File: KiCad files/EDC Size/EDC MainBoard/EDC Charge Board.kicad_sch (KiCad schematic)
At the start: 38 parts, among them IC2 TPS25730SRSMR, J1 USB_C_Receptacle_USB2.0_16P, J2 Conn_01x06, Q1 CSD87501L

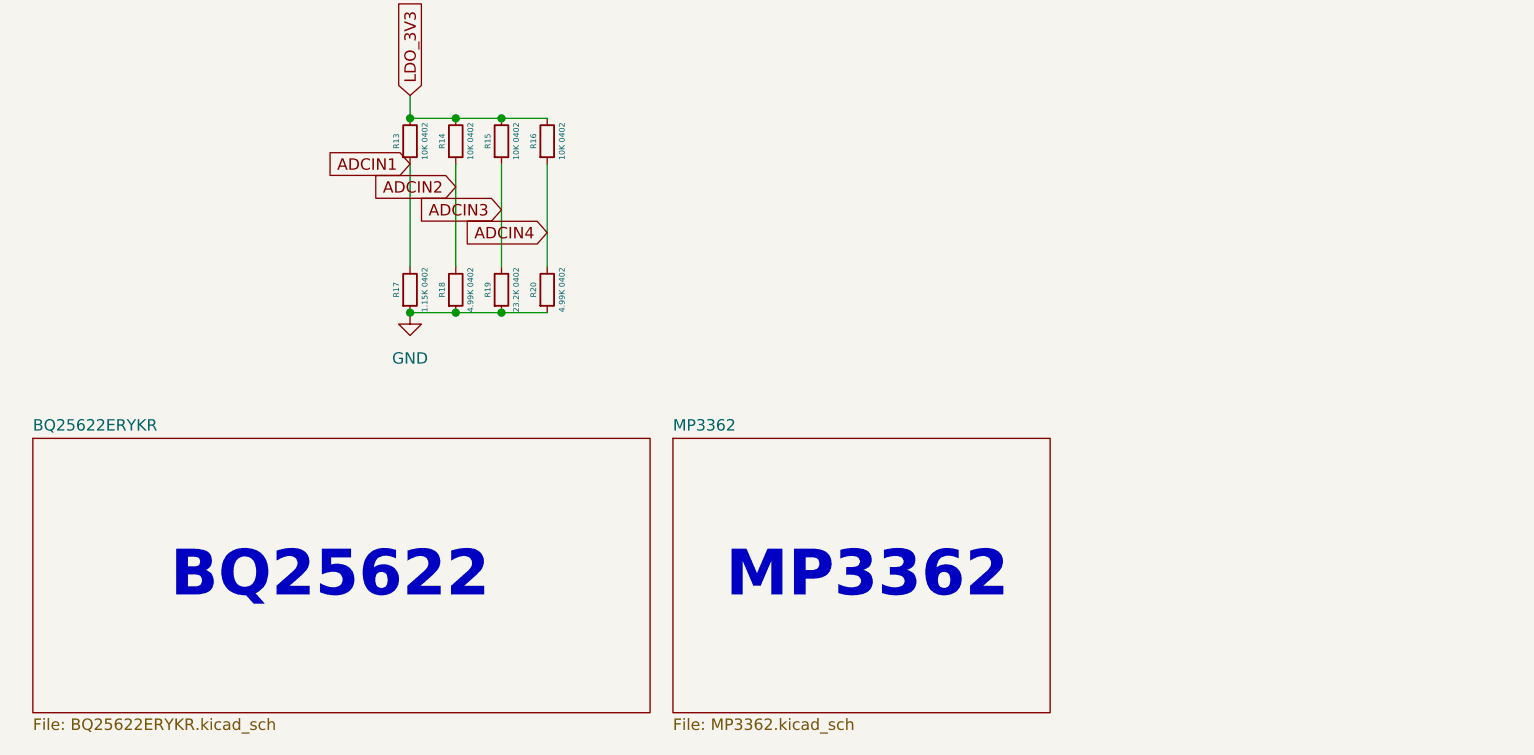
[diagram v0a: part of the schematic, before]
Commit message: updated the schematics and completed the battery charge IC circuit
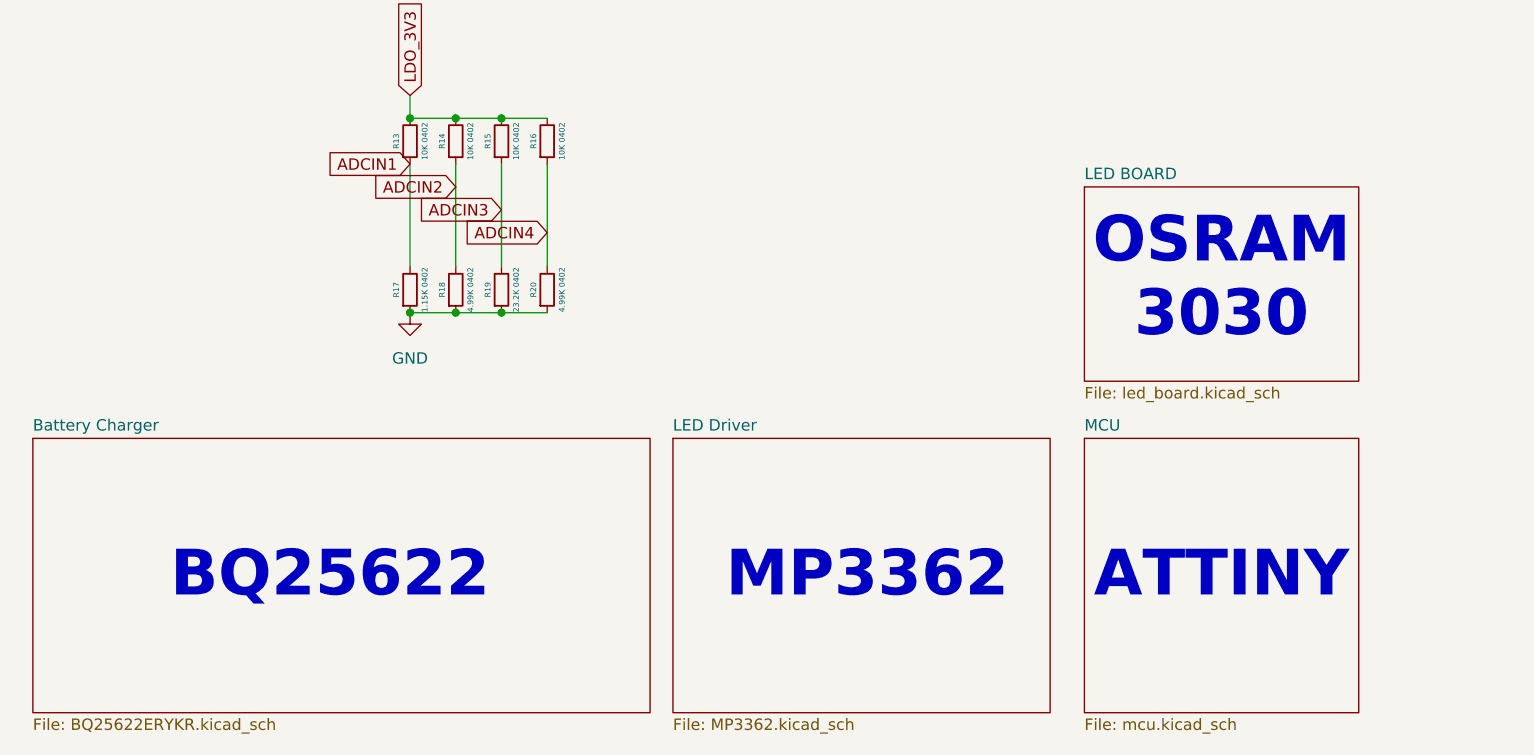
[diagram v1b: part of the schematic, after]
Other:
- sheet BQ25622ERYKR renamed Battery Charger
- sheet MP3362 renamed LED Driver
- added sheet LED BOARD (led_board.kicad_sch)
- added sheet MCU (mcu.kicad_sch)
- note added: "ATTINY"
- note added: "OSRAM 3030"
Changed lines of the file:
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@@
 		)
 	)
+	(text "OSRAM\n3030"
+		(exclude_from_sim no)
+		(at 149.86 139.7 0)
+		(effects
+			(font
+				(size 5.08 5.08)
+				(thickness 1.016)
+				(bold yes)
+			)
+		)
+	)
 	(text "MP3362"
 		(exclude_from_sim no)
@@
 		)
 	)
+	(text "ATTINY"
+		(exclude_from_sim no)
+		(at 149.86 172.72 0)
+		(effects
+			(font
+				(size 5.08 5.08)
+				(thickness 1.016)
+				(bold yes)
+			)
+		)
+	)
 	(text "BQ25622"
 		(exclude_from_sim no)
@@
 	(label "FAULT_IN"
 		(at 121.92 63.5 180)
-		(fields_autoplaced yes)
 		(effects
 			(font
@@
 	(label "FAULT_IN"
 		(at 251.46 55.88 0)
-		(fields_autoplaced yes)
 		(effects
 			(font
@@
 			(color 0 0 0 0.0000)
 		)
-		(property "Sheetname" "BQ25622ERYKR"
+		(property "Sheetname" "Battery Charger"
 			(at 17.78 156.7684 0)
 			(effects
@@
 	)
 	(sheet
+		(at 134.62 129.54)
+		(size 30.48 21.59)
+		(fields_autoplaced yes)
+		(stroke
+			(width 0.1524)
+			(type solid)
+		)
+		(fill
+			(color 0 0 0 0.0000)
+		)
+		(property "Sheetname" "LED BOARD"
+			(at 134.62 128.8284 0)
+			(effects
+				(font
+					(size 1.27 1.27)
+				)
+				(justify left bottom)
+			)
+		)
+		(property "Sheetfile" "led_board.kicad_sch"
+			(at 134.62 151.7146 0)
+			(effects
+				(font
+					(size 1.27 1.27)
+				)
+				(justify left top)
+			)
+		)
+		(instances
+			(project "EDC Charge Board"
+				(path "/e60e5011-22d9-49f2-91b7-a37b3d4aa83f"
+					(page "5")
+				)
+			)
+		)
+	)
+	(sheet
 		(at 88.9 157.48)
 		(size 41.91 30.48)
@@
 			(color 0 0 0 0.0000)
 		)
-		(property "Sheetname" "MP3362"
+		(property "Sheetname" "LED Driver"
 			(at 88.9 156.7684 0)
 			(effects
@@
 				)
 			)
+		)
+	)
+	(sheet
+		(at 134.62 157.48)
+		(size 30.48 30.48)
+		(fields_autoplaced yes)
+		(stroke
+			(width 0.1524)
+			(type solid)
+		)
+		(fill
+			(color 0 0 0 0.0000)
+		)
+		(property "Sheetname" "MCU"
+			(at 134.62 156.7684 0)
+			(effects
+				(font
+					(size 1.27 1.27)
+				)
+				(justify left bottom)
+			)
+		)
+		(property "Sheetfile" "mcu.kicad_sch"
+			(at 134.62 188.5446 0)
+			(effects
+				(font
+					(size 1.27 1.27)
+				)
+				(justify left top)
+			)
+		)
+		(instances
+			(project "EDC Charge Board"
+				(path "/e60e5011-22d9-49f2-91b7-a37b3d4aa83f"
+					(page "4")
+				)
+			)
